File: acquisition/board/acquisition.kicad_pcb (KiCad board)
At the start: 6 copper layers, 428 parts, among them J1 XILINX_JTAG, J10 MMCX, J11 MMCX, J12 MMCX, J13 MMCX, J14 MMCX, J15 MMCX, J16 MMCX, J17 MMCX, J18 UX60SX-MB-5ST, J19 CONN_01X05, J2 MMCX, J20 CONN_01X06, J3 MMCX, J4 MMCX, J5 MMCX, J6 MMCX, J7 MMCX, J8 MMCX, J9 MMCX, Q1 SSM6N58NU, Q2 SSM6N58NU, U1 AD9251, U10 FT232HL, U11 LMK04806, U12 AK5DAF1-100.0000T2, U14 74AVCH1T45, U15 74AVCH1T45, U16 74AVCH1T45, U17 74AVCH1T45, U18 74AVCH1T45, U19 74AVCH1T45, U2 XC7A50T-1FTG256C, U20 74AVCH1T45, U21 ECS-3225MVQ-120-CN-TR, U22 93LC56B-MS, U23 74AVCH1T45, U24 74AVCH1T45, U25 LTC3374-QFN, U26 LT3042, U27 LT3042, U28 ADR510, U29 SIP32408, U3 AD9251, U30 LDO1117-12, U4 AD9251, U5 AD9251, U6 ICE40UP5K_QFN48, U7 STM32L031-QFN32, U8 S27KS0642, U9 S25FL128SAGBHIA10

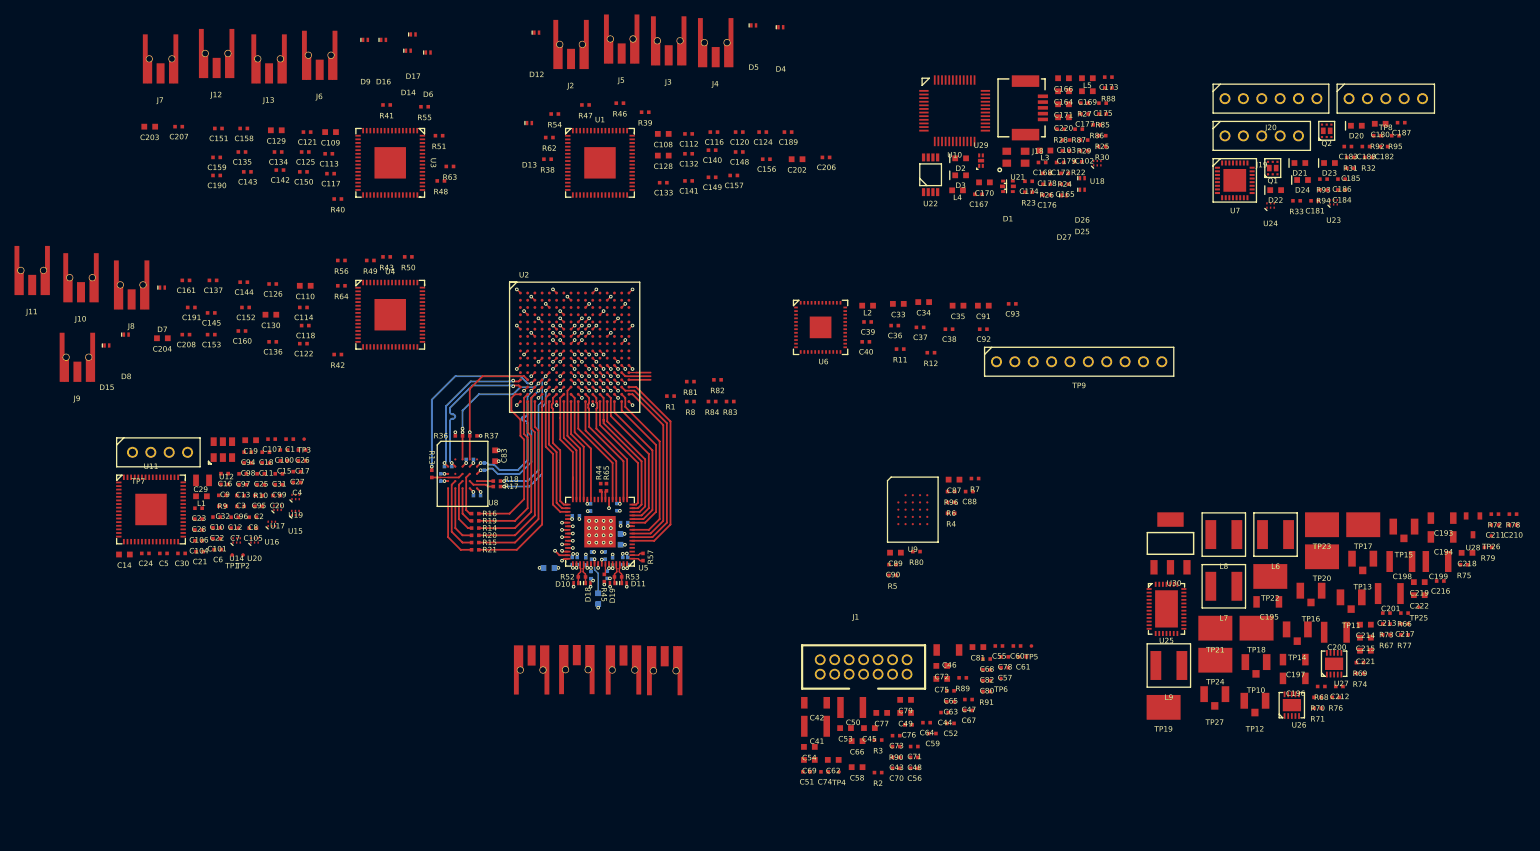
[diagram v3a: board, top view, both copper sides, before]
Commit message: Continued layout of bottom ADC, routed FPGA JTAG
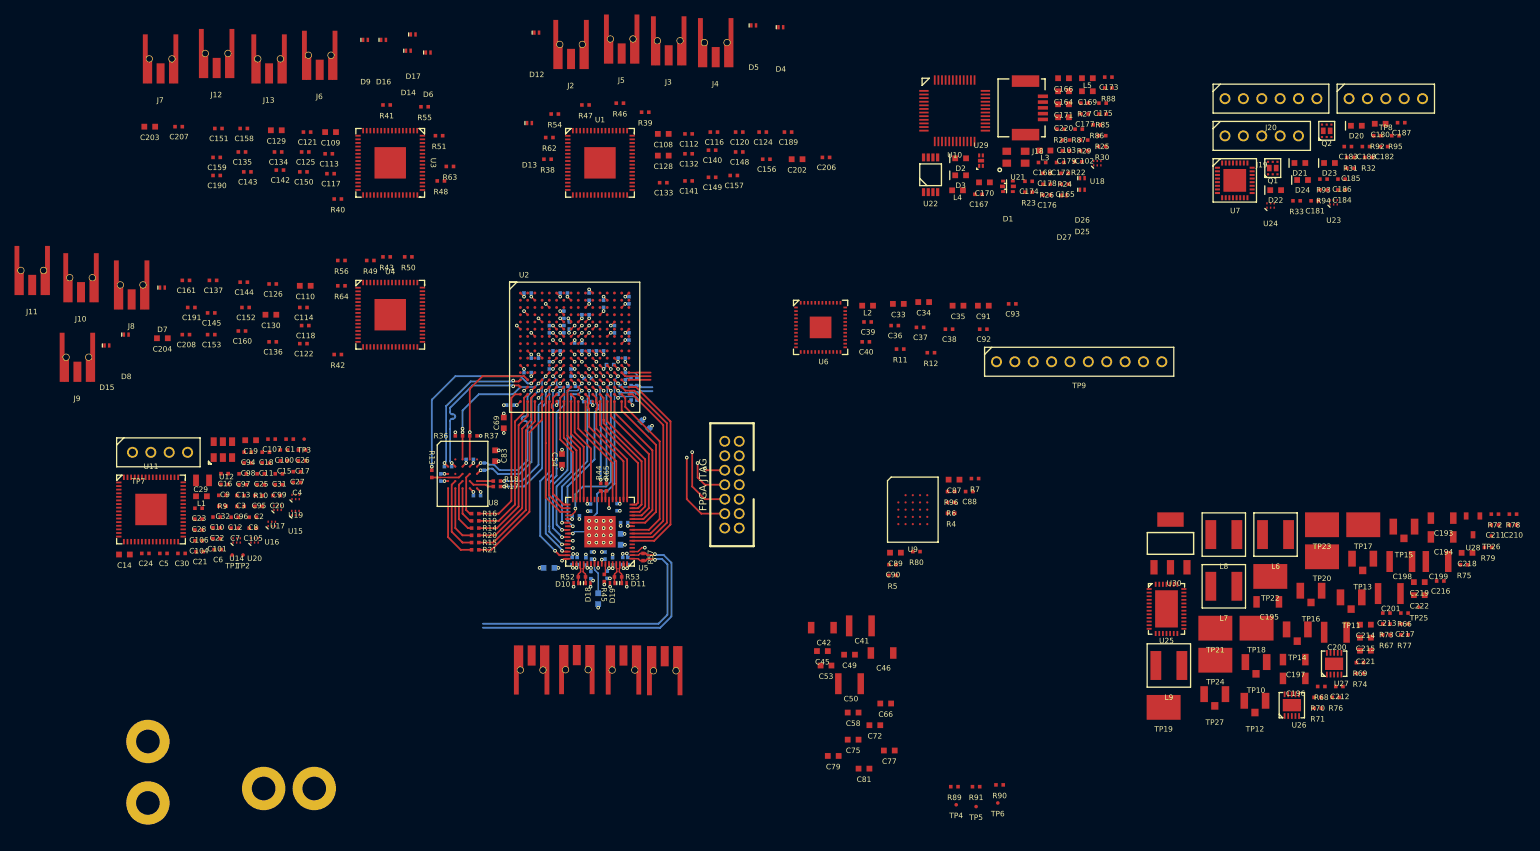
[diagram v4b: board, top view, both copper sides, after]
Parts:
- added MH1: HOLE_4x40, azonenberg_pcb:MECHANICAL_CLEARANCEHOLE_4_40, F.Cu at (48.5, 128.5)
- added MH2: HOLE_4x40, azonenberg_pcb:MECHANICAL_CLEARANCEHOLE_4_40, F.Cu at (41.5, 128.5)
- added MH3: HOLE_4x40, azonenberg_pcb:MECHANICAL_CLEARANCEHOLE_4_40, F.Cu at (25.5, 122.0)
- added MH4: HOLE_4x40, azonenberg_pcb:MECHANICAL_CLEARANCEHOLE_4_40, F.Cu at (25.5, 130.5)
- C43, C44, C47, C48, C51, C52, C55, C56, C57, C59, C60, C61, C62, C63, C64, C65, C67, C68, C70, C71, C73, C74, C76, C78, C80, C82, R1, R2, R3, R8, R81, R82, R83, R84: moved to B.Cu
- moved C55 81.4 mm to (78.0, 60.0)
- moved C61 79.6 mm to (81.0, 65.0), turned to 90 degrees
- moved C59 79.4 mm to (83.0, 60.0), turned to 180 degrees
- moved C70 77.7 mm to (83.0, 63.0), turned to 90 degrees
- moved C57 75.8 mm to (86.0, 63.0), turned to 180 degrees
- moved C48 75.4 mm to (78.0, 71.0), turned to 180 degrees
- moved C44 74.9 mm to (79.0, 69.0)
- moved C76 73.9 mm to (86.5, 60.5), turned to -90 degrees
- moved C71 73.7 mm to (82.0, 68.0)
- moved C65 73.2 mm to (83.0, 65.0), turned to -90 degrees
- moved C64 72.4 mm to (75.6, 75.5), turned to 180 degrees
- moved C43 72.4 mm to (81.0, 70.0), turned to -90 degrees
- moved C60 72.1 mm to (82.2, 74.5), turned to -90 degrees
- moved C73 72.1 mm to (88.5, 61.5), turned to 90 degrees
- moved C78 71.6 mm to (92.0, 61.0), turned to 90 degrees
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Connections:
- R81 pad 1: /ADCs/1V8 -> /D1V8
- R83 pad 1: /ADCs/1V8 -> /D1V8
- U2 pad C4: /ADCs/ADC3_CS_N -> /ADCs/ADC1_OE_N
- U2 pad E11: /ADCs/ADC_SCLK -> /ADCs/ICE40_SPI_SO
- U2 pad E13: /ADCs/ADC_SDIO -> /ADCs/ICE40_SPI_CS_N
- U2 pad M12: /ADCs/ICE40_SPI_CS_N -> /ADCs/ADC2_OE_N
- U2 pad M14: /ADCs/ICE40_SPI_SO -> /ADCs/D6_12
- U2 pad M6: /ADCs/D6_10 -> /ADCs/ADC_SDIO
- U2 pad N12: /ADCs/ADC2_OE_N -> /ADCs/ADC_SCLK
- U2 pad N6: /ADCs/D6_11 -> /ADCs/ADC3_OE_N
- U2 pad N9: /ADCs/D6_9 -> /ADCs/D6_13
- U2 pad P10: /ADCs/ADC1_OE_N -> /ADCs/D6_9
- U2 pad P11: /ADCs/D6_8 -> /ADCs/D6_10
- U2 pad P13: /ADCs/ADC3_OE_N -> /ADCs/D6_8
- U2 pad P6: /ADCs/D6_13 -> /ADCs/ADC3_CS_N
- U2 pad P9: /ADCs/D6_12 -> /ADCs/D6_11
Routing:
- net /GND: track 297.8 -> 348.3 mm, vias 83 -> 87
- net /ADCs/CLK3_N: track 1.60 -> 40.3 mm, vias 0 -> 1
- net /FPGA support/JTAG_TMS: track 0.71 -> 37.7 mm, vias 1 -> 2
- net /ADCs/CLK3_P: track 1.61 -> 38.5 mm, vias 0 -> 1
- net /FPGA support/JTAG_TCK: track 0.00 -> 36.3 mm, vias 0 -> 2
- net /D1V8: track 187.3 -> 220.7 mm, vias 40 -> 43
- net /FPGA support/JTAG_TDO: track 0.00 -> 32.7 mm, vias 0 -> 2
- net /FPGA support/JTAG_TDI: track 0.71 -> 32.1 mm, vias 1 -> 2
- net /ADCs/ADC_SDIO: track 0.80 -> 27.3 mm, vias 1 -> 2
- net /ADCs/D6_12: track 1.41 -> 27.6 mm
- net /ADCs/ADC_SCLK: track 0.70 -> 26.5 mm, vias 1 -> 2
- net /ADCs/ADC3_OE_N: track 2.73 -> 27.4 mm
- net /ADCs/ADC3_CS_N: track 0.85 -> 25.2 mm, vias 1 -> 2
- net /ADCs/D6_13: track 1.51 -> 25.6 mm
- net /ADCs/D6_11: track 0.80 -> 23.0 mm, vias 1 -> 2
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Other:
- board text added: "FPGA JTAG"

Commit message: Began layout of clocking subsystem
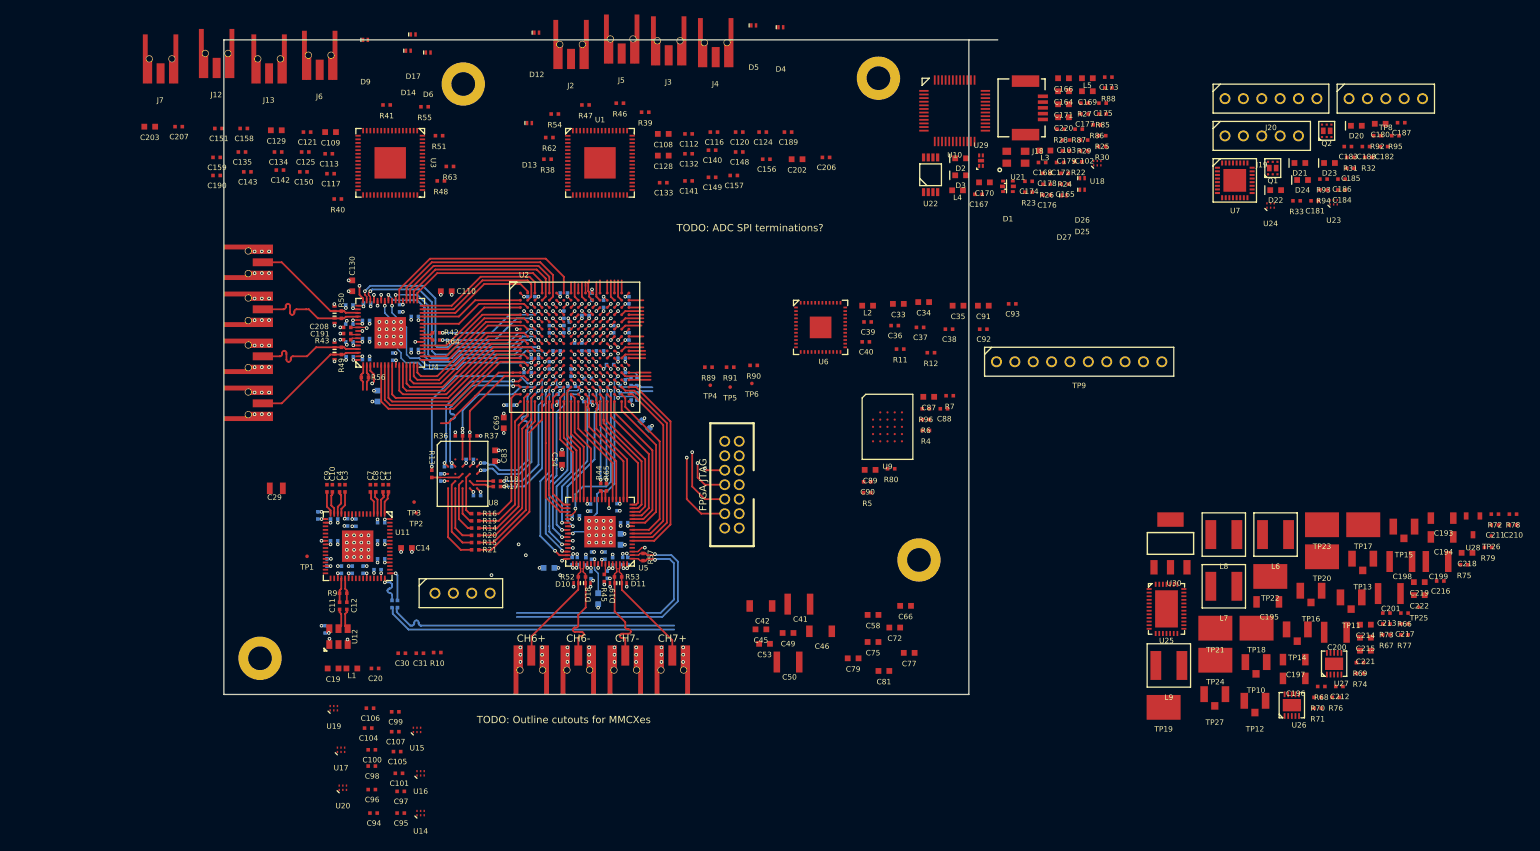
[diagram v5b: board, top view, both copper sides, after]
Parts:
- C114, C118, C122, C126, C13, C136, C137, C144, C145, C15, C152, C153, C16, C160, C161, C17, C18, C204, C21, C22, C23, C24, C25, C26, C27, C28, C32, C5, C6: moved to B.Cu
- moved MH2 129.9 mm to (126.5, 30.3)
- moved MH4 108.5 mm to (69.1, 31.1)
- moved MH1 89.4 mm to (132.1, 96.9)
- moved R89 67.2 mm to (103.0, 70.2)
- moved R90 67.2 mm to (109.2, 70.0)
- moved R91 67.2 mm to (106.0, 70.2)
- moved TP4 67.2 mm to (103.2, 72.8)
- moved TP5 67.2 mm to (106.0, 73.0)
- moved TP6 67.2 mm to (109.0, 72.5)
- moved C94 52.8 mm to (56.7, 131.9)
- moved C97 49.0 mm to (60.5, 128.9)
- moved C95 48.1 mm to (60.5, 131.9)
- moved TP7 46.1 mm to (69.0, 101.5)
- moved U14 45.5 mm to (63.2, 131.9)
- moved C98 45.3 mm to (56.5, 125.4)
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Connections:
- C11 pad 1: /Clocking/CLK_100MHZ_P -> /Clocking/CLK_100MHZ_N
- C12 pad 1: /Clocking/CLK_100MHZ_N -> /Clocking/CLK_100MHZ_P
- U2 pad A2: /ADCs/D5_2 -> /ADCs/D4_2
- U2 pad A3: /ADCs/D3_8 -> /ADCs/D4_4
- U2 pad A4: /ADCs/D3_6 -> /ADCs/D4_5
- U2 pad A5: /ADCs/D3_5 -> /ADCs/D4_7
- U2 pad A7: /ADCs/D3_2 -> /ADCs/D4_9
- U2 pad B1: /ADCs/D5_4 -> /ADCs/D4_1
- U2 pad B2: /ADCs/D5_1 -> /ADCs/D4_3
- U2 pad B4: /ADCs/D3_7 -> /ADCs/D4_6
- U2 pad B5: /ADCs/D3_4 -> /ADCs/D4_8
- U2 pad B6: /ADCs/D3_3 -> /ADCs/D5_1
- U2 pad B7: /ADCs/D3_1 -> /ADCs/D5_11
- U2 pad C1: /ADCs/D5_3 -> /ADCs/D3_13
- U2 pad C2: /ADCs/D5_0 -> /ADCs/D4_0
- U2 pad C3: /ADCs/D3_13 -> /ADCs/D5_3
- U2 pad C6: /ADCs/D3_10 -> /ADCs/D5_8
- U2 pad C7: /ADCs/D3_9 -> /ADCs/D5_7
- U2 pad D1: /ADCs/D5_6 -> /ADCs/D3_12
- U2 pad D5: /ADCs/D3_12 -> /ADCs/D5_6
- U2 pad D6: /ADCs/D3_11 -> /ADCs/D5_5
- U2 pad E1: /ADCs/D5_8 -> /ADCs/D3_10
- U2 pad E2: /ADCs/D5_5 -> /ADCs/D3_11
- U2 pad E5: /ADCs/ADC2_CS_N -> /ADCs/D5_0
- U2 pad E6: /ADCs/D3_0 -> /ADCs/D5_12
- U2 pad F2: /ADCs/D5_7 -> /ADCs/D3_9
- U2 pad G1: /ADCs/D5_12 -> /ADCs/D3_7
- U2 pad G2: /ADCs/D5_11 -> /ADCs/D3_8
- U2 pad G4: /ADCs/D5_10 -> /ADCs/ADC2_OE_N
- U2 pad H1: /ADCs/D4_4 -> /ADCs/D3_5
- U2 pad H2: /ADCs/D4_3 -> /ADCs/D3_6
- U2 pad H3: /ADCs/D4_6 -> /ADCs/D4_10
- U2 pad H4: /ADCs/D4_0 -> /ADCs/ADC2_CS_N
- U2 pad J1: /ADCs/D4_8 -> /ADCs/D3_3
- U2 pad J3: /ADCs/D4_5 -> /ADCs/D3_4
- U2 pad J4: /ADCs/D4_2 -> /ADCs/D4_12
- U2 pad J5: /ADCs/D4_1 -> /ADCs/D4_11
- U2 pad K1: /ADCs/D4_7 -> /ADCs/D3_1
- U2 pad K2: /ADCs/D4_12 -> /ADCs/D3_2
- U2 pad K3: /ADCs/D4_11 -> /ADCs/D4_13
- U2 pad K5: /ADCs/D4_13 -> /ADCs/D5_4
- U2 pad L2: /ADCs/D4_10 -> /ADCs/D3_0
- U2 pad L3: /ADCs/D4_9 -> /ADCs/D5_2
- U2 pad M12: /ADCs/ADC2_OE_N -> /ADCs/D5_10
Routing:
- net /GND: track 348.3 -> 667.4 mm, vias 87 -> 206
- net /3V3: track 0.00 -> 111.1 mm, vias 0 -> 15
- net /ADCs/ADC_SCLK: track 26.5 -> 96.9 mm, vias 2 -> 4
- net /VREF: track 14.1 -> 71.1 mm, vias 1 -> 5
- net /ADCs/ADC_SDIO: track 27.3 -> 82.6 mm, vias 2 -> 4
- net /ADCs/SYNC_2: track 0.00 -> 53.3 mm, vias 0 -> 1
- net /MCU/ADC2_PDWN: track 0.00 -> 50.0 mm, vias 0 -> 1
- net /ADCs/CLIP_3: track 0.00 -> 47.7 mm, vias 0 -> 1
- net /ADCs/CLIP_4: track 0.00 -> 45.8 mm, vias 0 -> 1
- net /ADCs/SYS_CLK_P: track 5.42 -> 46.1 mm
- net /ADCs/SYS_CLK_N: track 5.25 -> 45.9 mm
- net /ADCs/ADC2_CS_N: track 0.00 -> 34.5 mm, vias 0 -> 2
- net /ADCs/ADC2_OE_N: track 0.71 -> 35.0 mm, vias 1 -> 2
- net /D1V8: track 220.7 -> 253.8 mm, vias 43 -> 48
- net /ADCs/D4_12: track 0.00 -> 30.9 mm, vias 0 -> 2
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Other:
- board outline added: 107 x 90.5 mm
- board text added: "CH6+"
- board text added: "CH6-"
- board text added: "CH7+"
- board text added: "CH7-"
- board text added: "TODO: ADC SPI terminations?"
- board text added: "TODO: Outline cutouts for MMCXes"

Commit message: Continued layout of clocking subsystem, second ADC, and BGA fanout
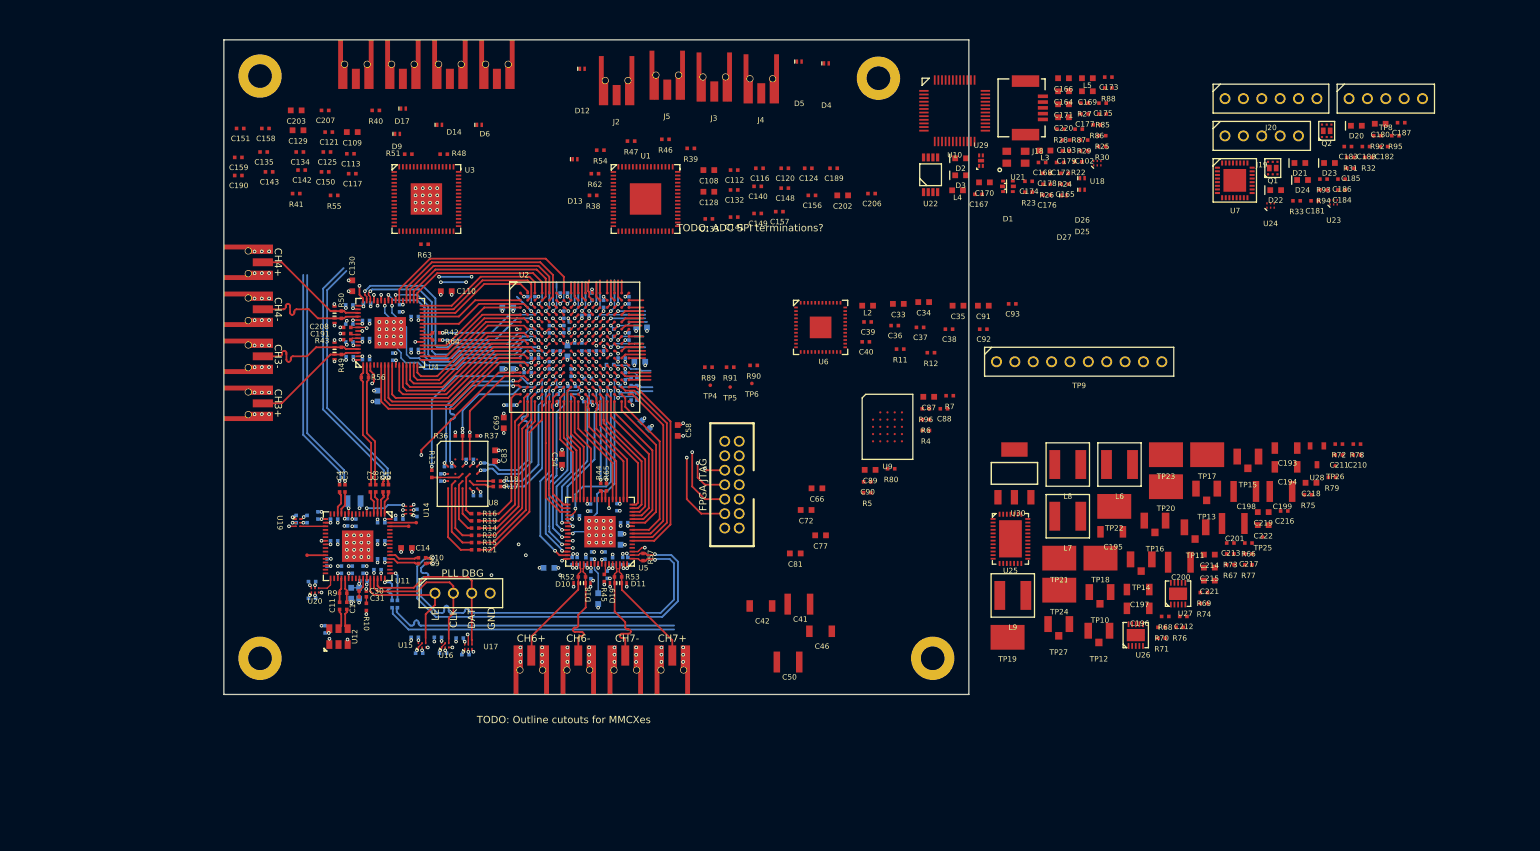
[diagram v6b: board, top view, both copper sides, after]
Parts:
- C100, C101, C104, C105, C106, C107, C19, C20, C29, C45, C49, C53, C75, C79, C94, C95, C96, C97, C98, C99, L1: moved to B.Cu
- moved C79 68.1 mm to (75.2, 62.0), turned to 180 degrees
- moved C75 63.1 mm to (75.2, 70.5)
- moved C49 49.5 mm to (83.5, 68.0), turned to -90 degrees
- moved C53 46.9 mm to (93.8, 64.8)
- moved U14 41.9 mm to (61.5, 90.0), turned to 90 degrees
- moved C94 41.9 mm to (62.7, 90.4), turned to 90 degrees
- moved C95 40.7 mm to (60.2, 91.2), turned to 180 degrees
- moved C45 40.6 mm to (93.5, 69.5)
- moved J7 40.0 mm to (67.2, 31.8)
- moved C58 37.1 mm to (98.8, 79.0), turned to 90 degrees
- moved C97 31.5 mm to (48.2, 99.9)
- moved C99 29.3 mm to (47.5, 91.2), turned to -90 degrees
- moved MH4 28.1 mm to (41.0, 30.0)
- moved C106 28.1 mm to (46.0, 91.2), turned to -90 degrees
- moved C96 27.7 mm to (48.2, 102.2)
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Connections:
- C1 pad 2: /ADCs/CLK0_P -> /ADCs/CLK1_P
- C2 pad 2: /ADCs/CLK0_N -> /ADCs/CLK1_N
- C3 pad 2: /ADCs/CLK2_P -> /ADCs/CLK0_P
- C4 pad 2: /ADCs/CLK2_N -> /ADCs/CLK0_N
- C7 pad 2: /ADCs/CLK1_P -> /ADCs/CLK2_P
- C8 pad 2: /ADCs/CLK1_N -> /ADCs/CLK2_N
- U11 pad 15: /Clocking/CLK3_AC_N -> unconnected-(U11-Pad15)
- U11 pad 16: /Clocking/CLK3_AC_P -> unconnected-(U11-Pad16)
- U11 pad 53: unconnected-(U11-Pad53) -> /Clocking/CLK3_AC_P
- U11 pad 54: unconnected-(U11-Pad54) -> /Clocking/CLK3_AC_N
- U2 pad D3: /ADCs/PLL_UWIRE_LE -> /ADCs/D5_13
- U2 pad H5: /ADCs/D5_13 -> /ADCs/PLL_UWIRE_LE
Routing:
- net /D1V8: track 253.8 -> 393.6 mm, vias 48 -> 58
- net /GND: track 667.4 -> 790.5 mm, vias 206 -> 245
- net /ADCs/A1V8_2: track 39.5 -> 128.5 mm
- net /CLK_4: track 0.00 -> 57.9 mm, vias 0 -> 1
- net /ADCs/PLL_UWIRE_LE: track 0.71 -> 53.6 mm, vias 1 -> 2
- net /PLL_STATUS_LD: track 0.00 -> 48.7 mm, vias 0 -> 1
- net /ADCs/PLL_UWIRE_CLK: track 0.71 -> 38.3 mm, vias 1 -> 2
- net /ADCs/CLK1_N: track 0.00 -> 34.7 mm, vias 0 -> 1
- net /PLL_SYNC: track 0.00 -> 34.6 mm, vias 0 -> 1
- net /ADCs/CLK1_P: track 0.00 -> 34.3 mm, vias 0 -> 1
- net /UWIRE_LEVELSHIFT_DIR: track 14.0 -> 47.9 mm, vias 0 -> 2
- net /ADCs/PLL_UWIRE_DATA: track 0.71 -> 34.3 mm, vias 1 -> 2
- net /ADCs/D5_10: track 0.71 -> 33.9 mm, vias 1 -> 2
- net /ADCs/CLK0_P: track 0.00 -> 31.2 mm, vias 0 -> 1
- net /ADCs/CLK0_N: track 0.00 -> 31.2 mm, vias 0 -> 1
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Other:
- board size 107 x 90.5 mm -> 103 x 90.5 mm
- board text added: "CH3+"
- board text added: "CH3-"
- board text added: "CH4+"
- board text added: "CH4-"
- board text added: "CLK"
- board text added: "DAT"
- board text added: "GND"
- board text added: "LE"
- board text added: "PLL DBG"

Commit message: Hooked up power and analog connections to third ADC, no data bus yet
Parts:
- C113, C117, C121, C125, C134, C135, C142, C143, C150, C151, C158, C159, C203, C207: moved to B.Cu
- moved C159 30.3 mm to (68.2, 41.5), turned to 180 degrees
- moved C135 26.4 mm to (67.8, 43.7), turned to 90 degrees
- moved C190 26.3 mm to (64.2, 41.0), turned to 90 degrees
- moved C129 26.2 mm to (72.1, 41.7), turned to 90 degrees
- moved C151 24.4 mm to (61.8, 43.6), turned to 90 degrees
- moved C143 24.0 mm to (66.2, 43.7), turned to 90 degrees
- moved C158 23.9 mm to (64.8, 43.7), turned to -90 degrees
- moved R40 20.1 mm to (63.9, 53.6), turned to -90 degrees
- moved C121 19.9 mm to (67.3, 48.3), turned to 180 degrees
- moved C125 18.8 mm to (66.2, 50.4), turned to 90 degrees
- moved R41 18.1 mm to (63.4, 41.0), turned to 90 degrees
- moved C207 17.0 mm to (65.2, 42.4)
- moved C134 17.0 mm to (63.1, 43.7), turned to -90 degrees
- moved C142 13.6 mm to (60.3, 43.6), turned to -90 degrees
- moved C203 13.3 mm to (58.0, 40.5), turned to 90 degrees
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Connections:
- U2 pad C12: /ADCs/PLL_UWIRE_CLK -> /ADCs/D5_2
- U2 pad C13: /ADCs/PLL_UWIRE_DATA -> /ADCs/D5_4
- U2 pad K5: /ADCs/D5_4 -> /ADCs/PLL_UWIRE_CLK
- U2 pad L3: /ADCs/D5_2 -> /ADCs/PLL_UWIRE_DATA
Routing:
- net /GND: track 790.5 -> 930.1 mm, vias 245 -> 290
- net /ADCs/CLK0_N: track 31.2 -> 74.7 mm
- net /ADCs/CLK0_P: track 31.2 -> 73.8 mm
- net /ADCs/SYS_CLK_P: track 46.1 -> 84.0 mm
- net /ADCs/SYS_CLK_N: track 45.9 -> 83.7 mm
- net /D1V8: track 393.6 -> 422.1 mm, vias 58 -> 62
- net /VREF: track 79.7 -> 107.4 mm, vias 5 -> 7
- net /ADCs/ADC_SDIO: track 89.0 -> 113.8 mm, vias 4 -> 5
- net /ADCs/ADC_SCLK: track 100.1 -> 123.9 mm, vias 4 -> 5
- net /ADCs/CLK1_P: track 34.3 -> 57.7 mm, vias 1 -> 2
- net /ADCs/CLK1_N: track 34.7 -> 57.7 mm, vias 1 -> 2
- net /ADCs/D5_4: track 24.0 -> 3.96 mm
- net /ADCs/A1V8_1: track 0.00 -> 19.8 mm, vias 0 -> 10
- net /ADCs/IN5_P: track 0.00 -> 15.1 mm
- net /ADCs/IN2_P: track 0.00 -> 15.1 mm
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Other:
- board text added: "CH2+"
- board text added: "CH2-"
- board text added: "CH5+"
- board text added: "CH5-"
